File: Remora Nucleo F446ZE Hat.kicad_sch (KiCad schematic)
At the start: 9 parts, among them J1 NucleoF446ZE CN11 Header, J2 NucleoF446ZE CN12 Header, J3 5V_SUPPLY, J4 5V_AUXOUT

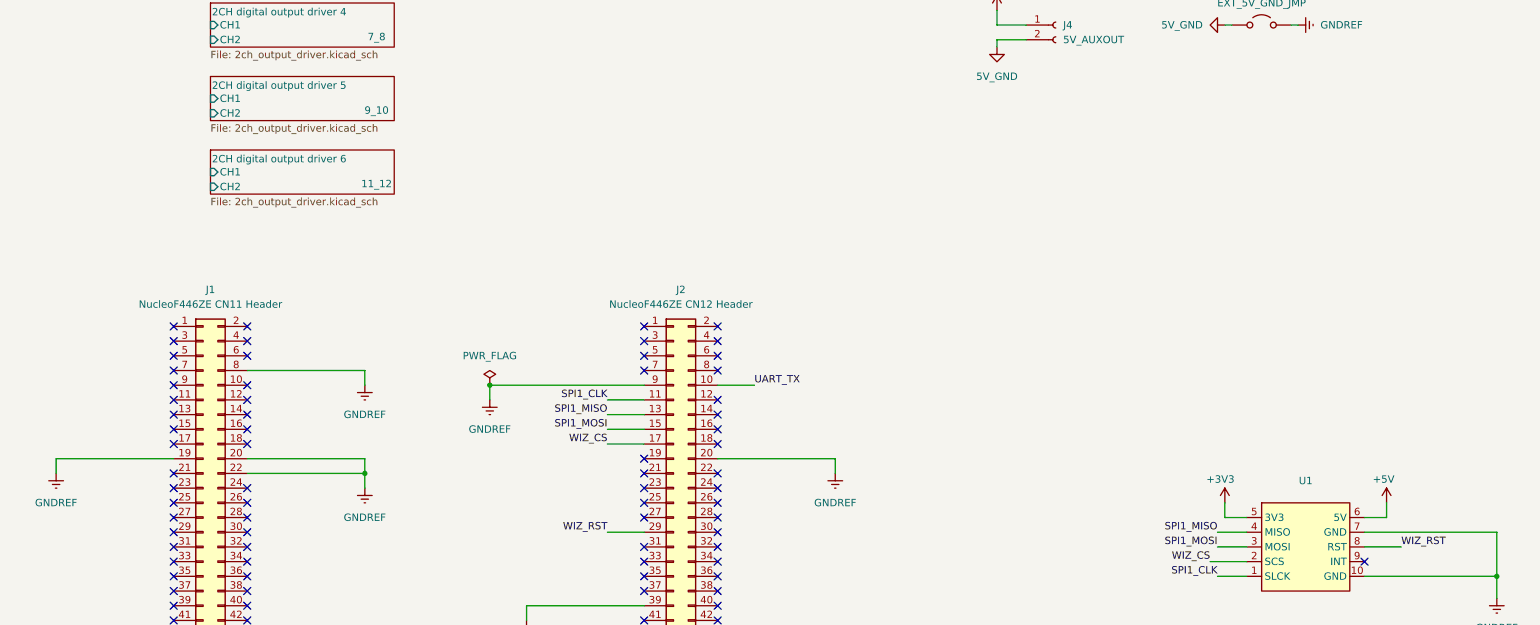
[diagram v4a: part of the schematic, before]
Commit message: added reset button, programmable user button, user LED and updates to todos
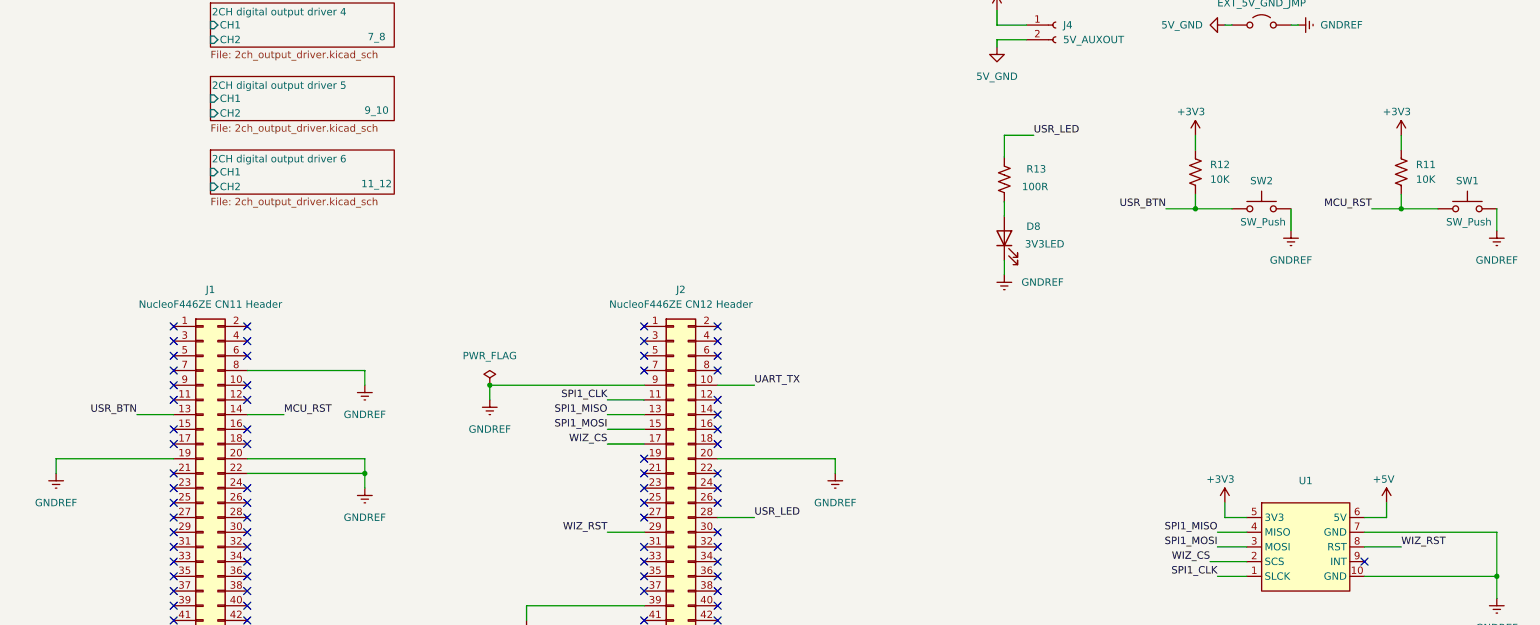
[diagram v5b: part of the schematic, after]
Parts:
- added D8: 3V3LED, Diode_SMD:D_1206_3216Metric_Pad1.42x1.75mm_HandSolder, symbol Device:LED
- added R11, R12: 10K, symbol Device:R_US
- added R13: 100R, Resistor_SMD:R_1206_3216Metric_Pad1.30x1.75mm_HandSolder, symbol Device:R_US
- added SW1, SW2: SW_Push, symbol Switch:SW_Push
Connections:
- net +3V3: now also R11.1, R12.1
- net GNDREF: now also D8.1 (K), SW1.2, SW2.2
- net USR_LED: now reaches J2.28 (Pin_28)
- net USR_LED: now also R13.1
- net USR_BTN: now reaches J1.13 (Pin_13)
- net USR_BTN: now also R12.2, SW2.1
- net MCU_RST: now reaches J1.14 (Pin_14)
- net MCU_RST: now also R11.2, SW1.1
- new net: D8.2 (A), R13.2
- no-connect marks 109 -> 106

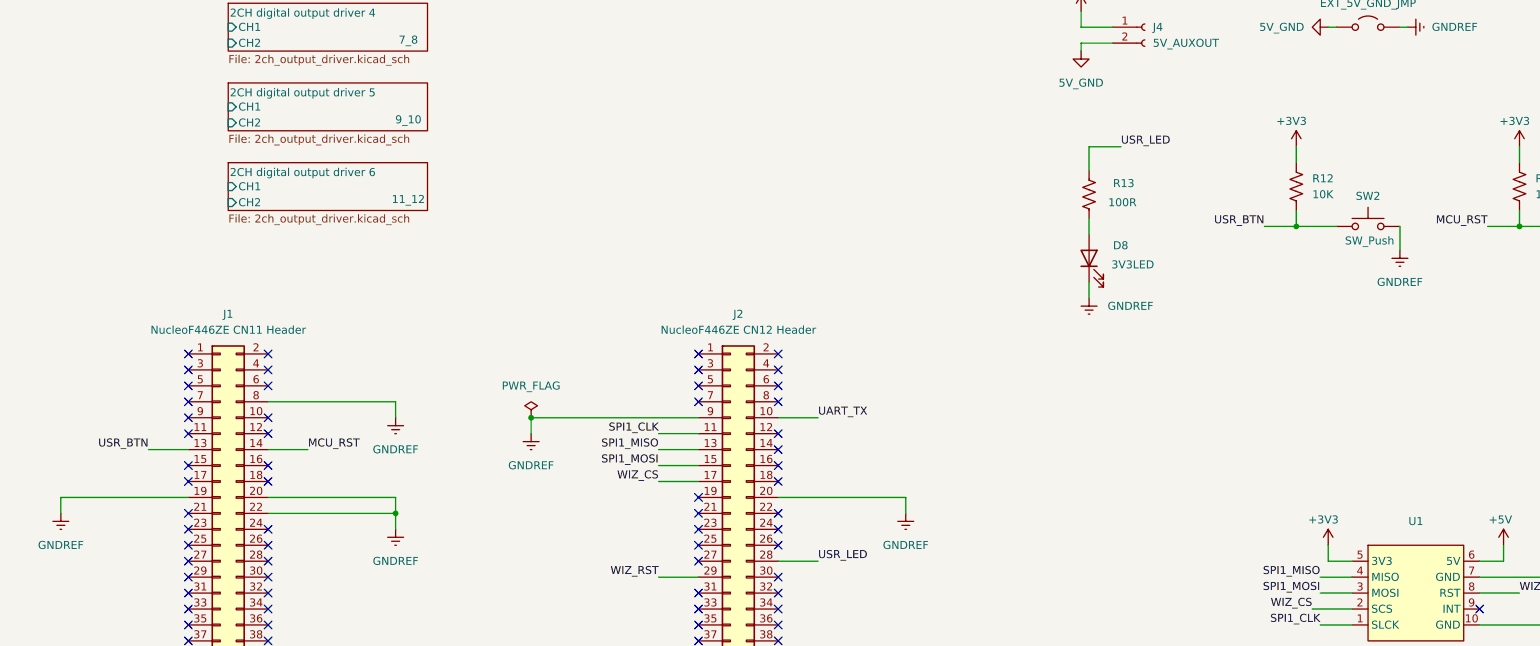
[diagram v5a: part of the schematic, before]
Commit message: fixed error in placement of usr_button and pull down config
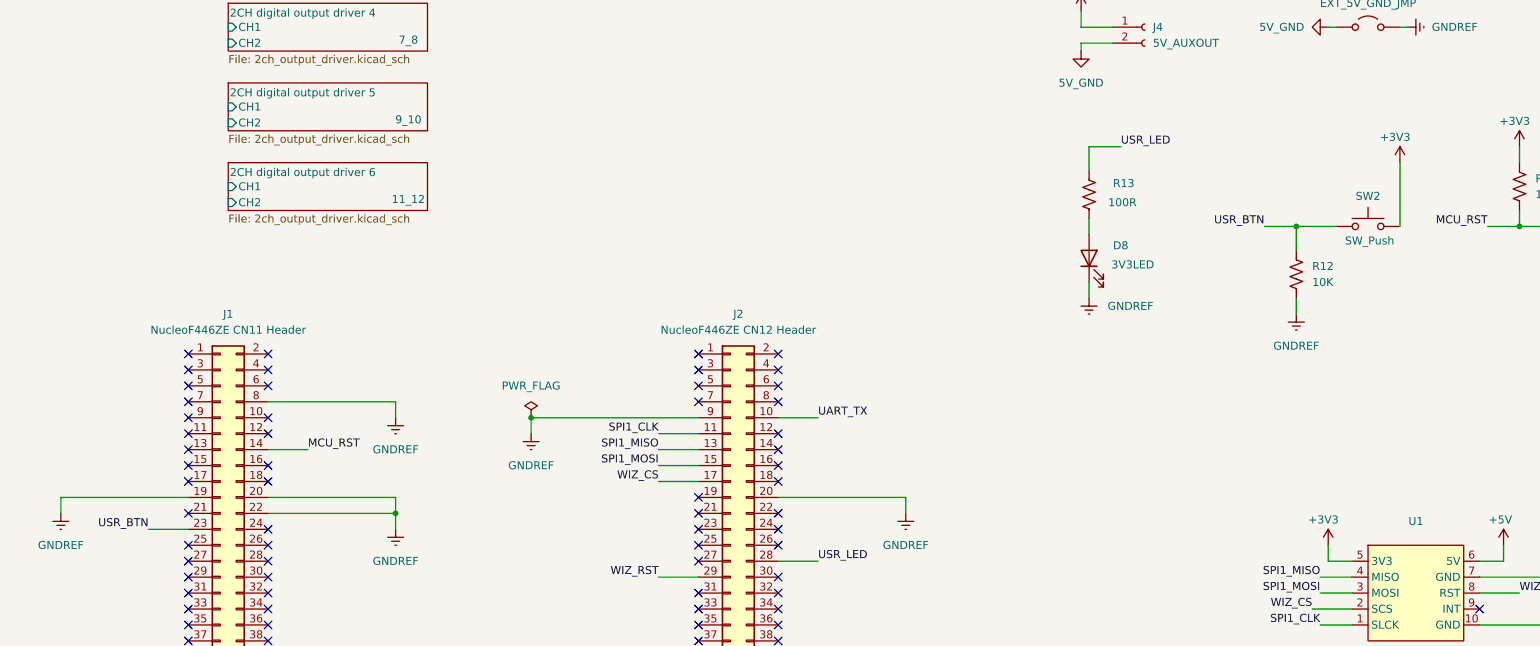
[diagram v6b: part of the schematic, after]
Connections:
- net +3V3: now also SW2.2; no longer R12.1
- net GNDREF: now also R12.2; no longer SW2.2
- net USR_BTN: now also J1.23 (Pin_23), R12.1; no longer J1.13 (Pin_13), R12.2
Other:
- moved on the sheet: R12
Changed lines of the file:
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@@
+	)
+	(junction
+		(at 223.52 90.17)
+		(diameter 0)
+		(color 0 0 0 0)
 	)
 	(junction
@@
 	)
 	(junction
-		(at 223.52 90.17)
-		(diameter 0)
-		(color 0 0 0 0)
-	)
-	(junction
 		(at 80.01 135.89)
 		(diameter 0)
@@
 	)
 	(no_connect
-		(at 46.99 138.43)
-	)
-	(no_connect
 		(at 140.97 153.67)
 	)
@@
 	)
 	(no_connect
+		(at 46.99 125.73)
+	)
+	(no_connect
 		(at 59.69 156.21)
 	)
@@
 	(wire
 		(pts
-			(xy 223.52 87.63) (xy 223.52 90.17)
-		)
-		(stroke
-			(width 0)
-			(type default)
-		)
-	)
-	(wire
-		(pts
 			(xy 254 90.17) (xy 259.08 90.17)
 		)
@@
 	(wire
 		(pts
+			(xy 223.52 90.17) (xy 229.87 90.17)
+		)
+		(stroke
+			(width 0)
+			(type default)
+		)
+	)
+	(wire
+		(pts
 			(xy 140.97 143.51) (xy 147.32 143.51)
 		)
@@
 	(wire
 		(pts
+			(xy 223.52 101.6) (xy 223.52 104.14)
+		)
+		(stroke
+			(width 0)
+			(type default)
+		)
+	)
+	(wire
+		(pts
 			(xy 228.6 58.42) (xy 229.87 58.42)
 		)
@@
 	(wire
 		(pts
-			(xy 223.52 77.47) (xy 223.52 80.01)
+			(xy 240.03 80.01) (xy 240.03 90.17)
 		)
 		(stroke
@@
 	(wire
 		(pts
-			(xy 40.64 125.73) (xy 46.99 125.73)
+			(xy 40.64 138.43) (xy 46.99 138.43)
 		)
 		(stroke
@@
 	(wire
 		(pts
-			(xy 240.03 90.17) (xy 240.03 93.98)
-		)
-		(stroke
-			(width 0)
-			(type default)
-		)
-	)
-	(wire
-		(pts
 			(xy 101.6 120.65) (xy 101.6 123.19)
 		)
@@
 	(wire
 		(pts
-			(xy 223.52 90.17) (xy 229.87 90.17)
+			(xy 223.52 90.17) (xy 223.52 93.98)
 		)
 		(stroke
@@
 	)
 	(label "USR_BTN"
-		(at 40.64 125.73 180)
+		(at 40.64 138.43 180)
 		(effects
 			(font
@@
 	(symbol
 		(lib_id "power:GNDREF")
-		(at 240.03 93.98 0)
+		(at 223.52 104.14 0)
 		(unit 1)
 		(exclude_from_sim no)
@@
 		(fields_autoplaced yes)
 		(property "Reference" "#PWR0149"
-			(at 240.03 100.33 0)
+			(at 223.52 110.49 0)
 			(effects
 				(font
@@
 		)
 		(property "Value" "GNDREF"
-			(at 240.03 99.06 0)
+			(at 223.52 109.22 0)
 			(effects
 				(font
@@
 		)
 		(property "Footprint" ""
-			(at 240.03 93.98 0)
+			(at 223.52 104.14 0)
 			(effects
 				(font
@@
 		)
 		(property "Datasheet" ""
-			(at 240.03 93.98 0)
+			(at 223.52 104.14 0)
 			(effects
 				(font
@@
 		)
 		(property "Description" "Power symbol creates a global label with name \"GNDREF\" , reference supply ground"
-			(at 240.03 93.98 0)
+			(at 223.52 104.14 0)
 			(effects
 				(font
@@
 	(symbol
 		(lib_id "Device:R_US")
-		(at 223.52 83.82 0)
+		(at 223.52 97.79 0)
 		(unit 1)
 		(exclude_from_sim no)
@@
 		(fields_autoplaced yes)
 		(property "Reference" "R12"
-			(at 226.06 82.5499 0)
+			(at 226.06 96.5199 0)
 			(effects
 				(font
@@
 		)
 		(property "Value" "10K"
-			(at 226.06 85.0899 0)
+			(at 226.06 99.0599 0)
 			(effects
 				(font
@@
 		)
 		(property "Footprint" ""
-			(at 224.536 84.074 90)
+			(at 224.536 98.044 90)
 			(effects
 				(font
@@
 		)
 		(property "Datasheet" "~"
-			(at 223.52 83.82 0)
+			(at 223.52 97.79 0)
 			(effects
 				(font
@@
 		)
 		(property "Description" "Resistor, US symbol"
-			(at 223.52 83.82 0)
+			(at 223.52 97.79 0)
 			(effects
 				(font
@@
 	(symbol
 		(lib_id "power:+3V3")
-		(at 223.52 77.47 0)
+		(at 240.03 80.01 0)
 		(unit 1)
 		(exclude_from_sim no)
@@
 		(dnp no)
 		(property "Reference" "#PWR0148"
-			(at 223.52 81.28 0)
+			(at 240.03 83.82 0)
 			(effects
 				(font
@@
 		)
 		(property "Value" "+3V3"
-			(at 222.758 73.406 0)
+			(at 239.268 75.946 0)
 			(effects
 				(font
@@
 		)
 		(property "Footprint" ""
-			(at 223.52 77.47 0)
+			(at 240.03 80.01 0)
 			(effects
 				(font
@@
 		)
 		(property "Datasheet" ""
-			(at 223.52 77.47 0)
+			(at 240.03 80.01 0)
 			(effects
 				(font
@@
 		)
 		(property "Description" "Power symbol creates a global label with name \"+3V3\""
-			(at 223.52 77.47 0)
-			(effects
-				(font
+			(at 240.03 80.01 0)
+			(effects
+				(font

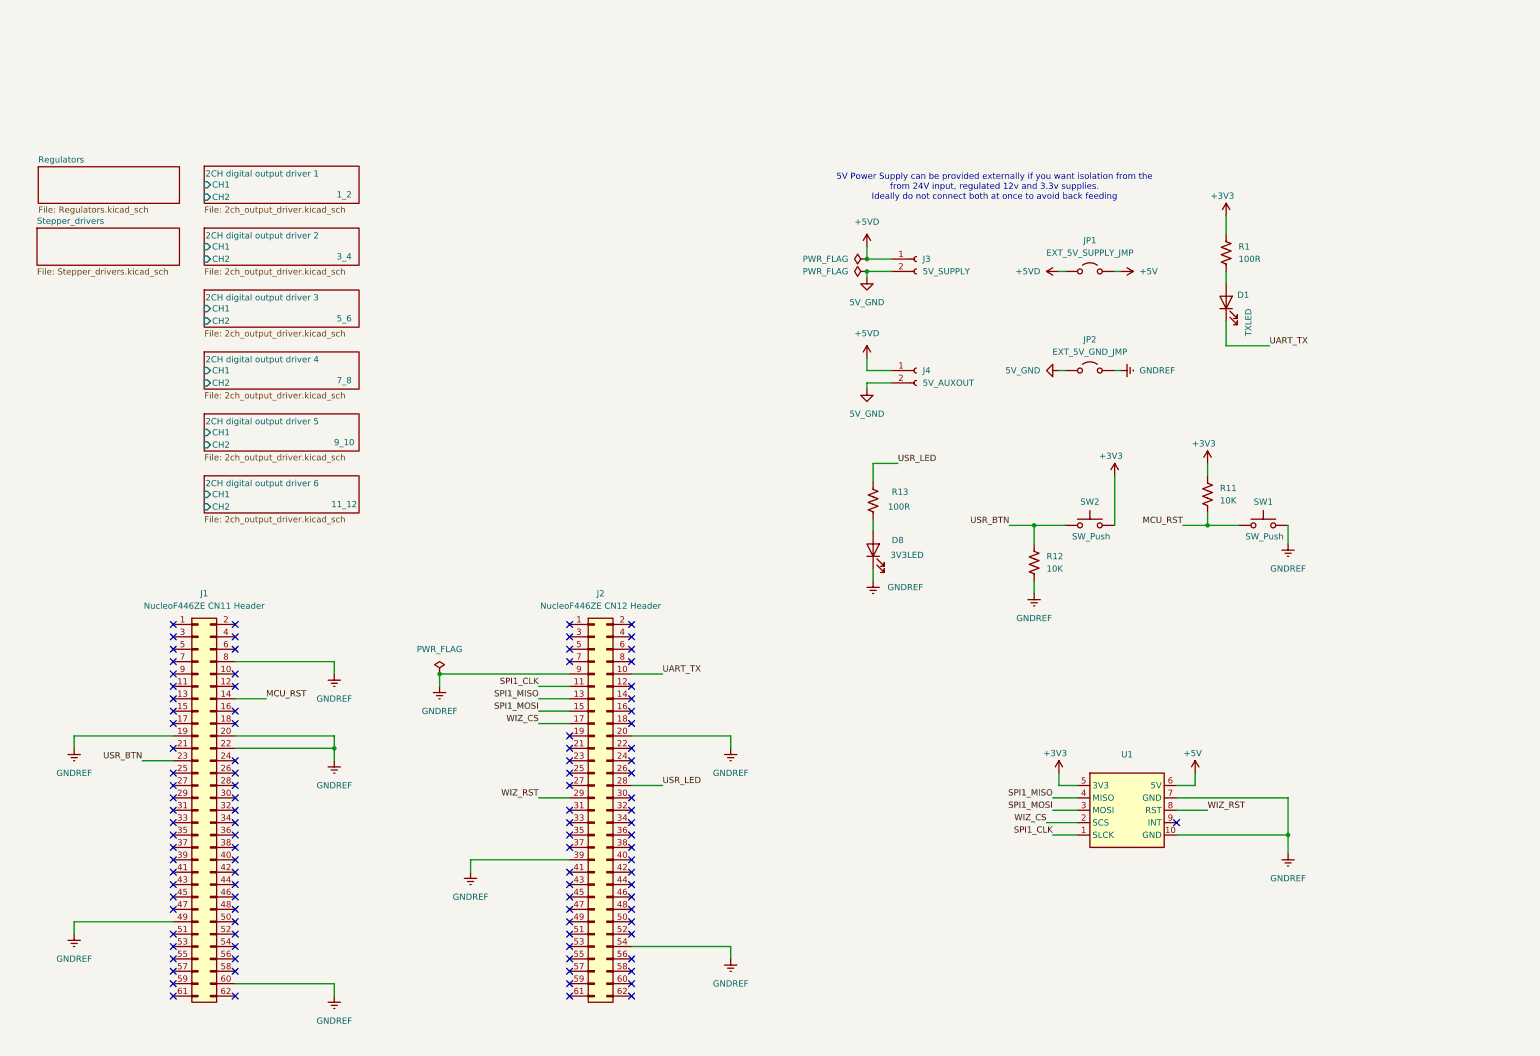
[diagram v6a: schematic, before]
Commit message: redrew stepper drivers as duplicatable heirarchical sheets, moved jumpers into power managemente sheet, moved LEDs and user buttons into own sheet to save space. Fixed a few random labelling issues.
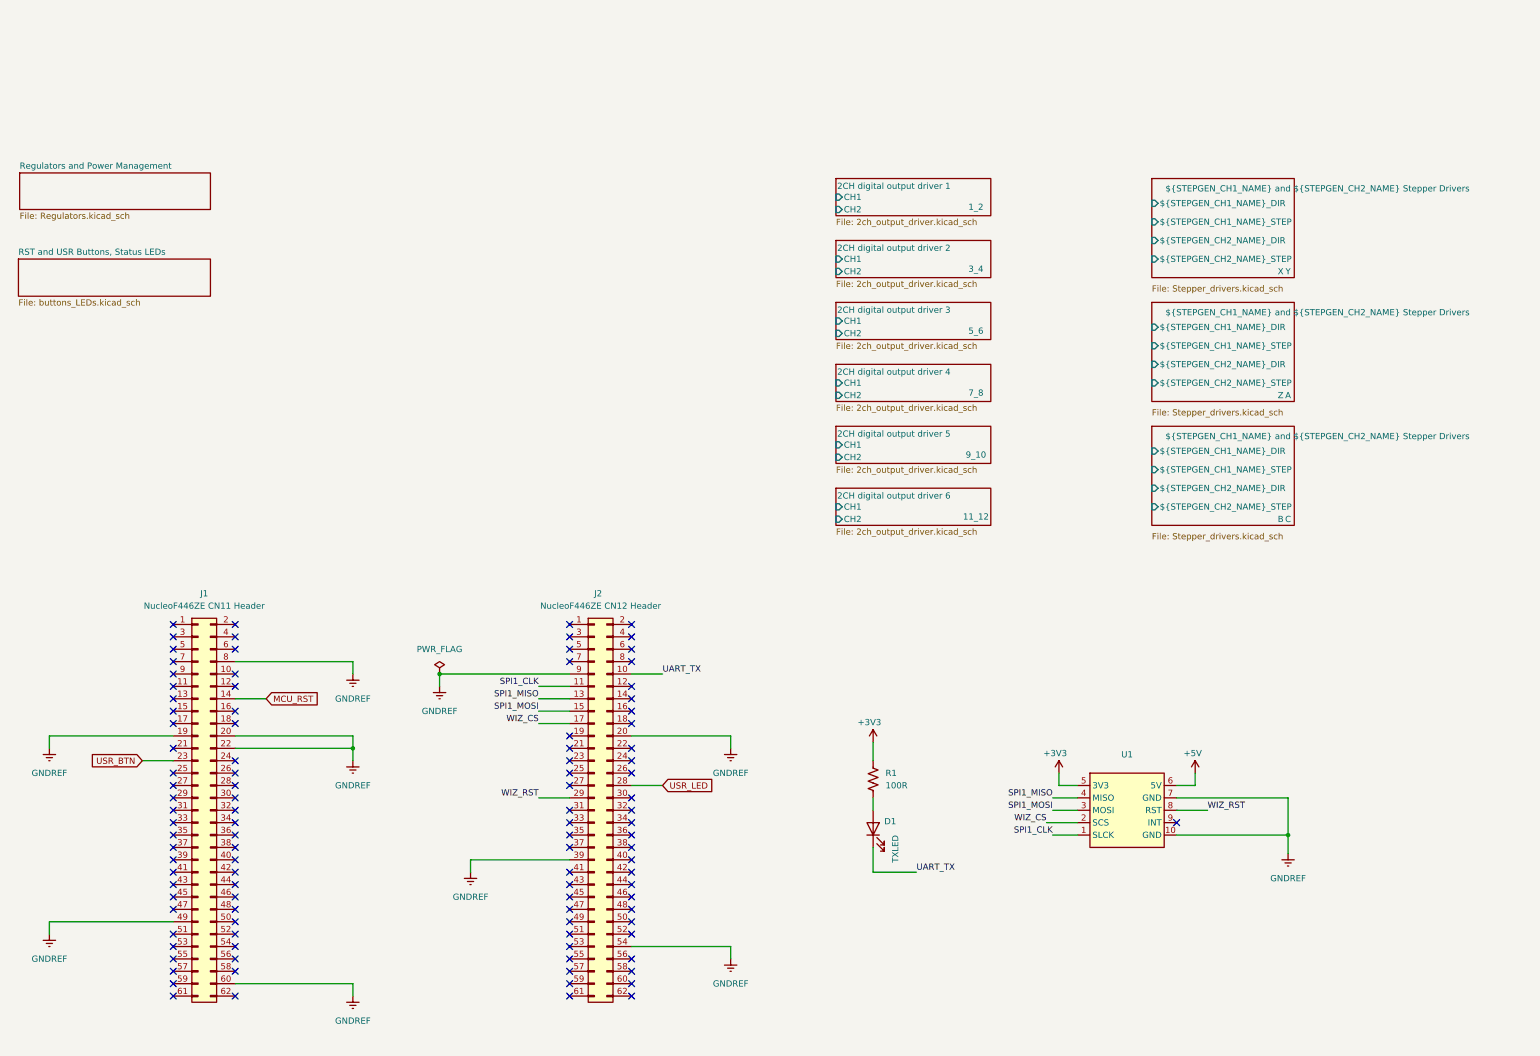
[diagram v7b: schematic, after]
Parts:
- removed D8: 3V3LED, Diode_SMD:D_1206_3216Metric_Pad1.42x1.75mm_HandSolder, symbol Device:LED
- removed J3: 5V_SUPPLY, symbol Connector:Conn_01x02_Socket
- removed J4: 5V_AUXOUT, symbol Connector:Conn_01x02_Socket
- removed JP1: EXT_5V_SUPPLY_JMP, Jumper:SolderJumper-2_P1.3mm_Open_TrianglePad1.0x1.5mm, symbol Jumper:Jumper_2_Open
- removed JP2: EXT_5V_GND_JMP, Jumper:SolderJumper-2_P1.3mm_Open_TrianglePad1.0x1.5mm, symbol Jumper:Jumper_2_Open
- removed R11, R12: 10K, symbol Device:R_US
- removed R13: 100R, Resistor_SMD:R_1206_3216Metric_Pad1.30x1.75mm_HandSolder, symbol Device:R_US
- removed SW1, SW2: SW_Push, symbol Switch:SW_Push
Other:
- sheet Regulators renamed Regulators and Power Management
- removed sheet Stepper_drivers
- added sheet ${STEPGEN_CH1_NAME} and ${STEPGEN_CH2_NAME} Stepper Drivers (Stepper_drivers.kicad_sch)
- added sheet RST and USR Buttons, Status LEDs (buttons_LEDs.kicad_sch)
- note removed: "5V Power Supply can be provided externally if you want isolation from the from 24V input, regulated 12v and 3.3v supplies. Ideally do not connect both at once to avoid back feeding"
- moved on the sheet: D1, R1
